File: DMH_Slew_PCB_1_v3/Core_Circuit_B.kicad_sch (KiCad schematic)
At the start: 48 parts, among them J6 TS_Jack_6.35mm_Sw, J60 Conn_01x08_PinHeader, J61 Conn_01x08_PinHeader, J7 TS_Jack_6.35mm_Sw, J8 TS_Jack_6.35mm_Sw, Q10 BC558, Q7 BC548, Q8 BC548, Q9 BC558, SW4 SW_DPDT_3way, SW5 SW_DPDT, SW6 SPDT_OnOffOn, U3 TL074, U4 TL074

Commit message: V3 sch redesign ongoing
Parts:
- removed J60, J61: Conn_01x08_PinHeader, Connector_PinHeader_2.54mm:PinHeader_1x08_P2.54mm_Vertical, symbol SynthStuff:Conn_01x08_PinHeader
- removed R69, R70: 1k, Resistor_THT:R_Axial_DIN0207_L6.3mm_D2.5mm_P7.62mm_Horizontal, symbol Device:R_US
- removed R71, R72: 100k, Resistor_THT:R_Axial_DIN0207_L6.3mm_D2.5mm_P7.62mm_Horizontal, symbol Device:R_US
- removed R73: 220k, Resistor_THT:R_Axial_DIN0207_L6.3mm_D2.5mm_P7.62mm_Horizontal, symbol Device:R_US
- removed R74: 10k, Resistor_THT:R_Axial_DIN0207_L6.3mm_D2.5mm_P7.62mm_Horizontal, symbol Device:R_US
- removed R75, R76: 1k8, Resistor_THT:R_Axial_DIN0207_L6.3mm_D2.5mm_P7.62mm_Horizontal, symbol Device:R_US
- added C17: 10pF, Capacitor_THT:C_Disc_D3.0mm_W2.0mm_P2.50mm, symbol Device:C
- added C18: 220nF, Capacitor_THT:C_Disc_D4.3mm_W1.9mm_P5.00mm, symbol Device:C
- added C19: 22nF, Capacitor_THT:C_Disc_D4.3mm_W1.9mm_P5.00mm, symbol Device:C
- added C20: 2.2nF, Capacitor_THT:C_Disc_D4.3mm_W1.9mm_P5.00mm, symbol Device:C
- added R41: 56k, Resistor_THT:R_Axial_DIN0207_L6.3mm_D2.5mm_P7.62mm_Horizontal, symbol Device:R_US
- added R42, R43, R44, R56: 100k, Resistor_THT:R_Axial_DIN0207_L6.3mm_D2.5mm_P7.62mm_Horizontal, symbol Device:R_US
- added R55: 220k, Resistor_THT:R_Axial_DIN0207_L6.3mm_D2.5mm_P7.62mm_Horizontal, symbol Device:R_US
- added R61, R62: 1k, Resistor_THT:R_Axial_DIN0207_L6.3mm_D2.5mm_P7.62mm_Horizontal, symbol Device:R_US
- added unit 5 of U3
- added unit 5 of U4
- C22: value 220nF -> 10pF; footprint Capacitor_THT:C_Disc_D4.3mm_W1.9mm_P5.00mm -> Capacitor_THT:C_Disc_D3.0mm_W2.0mm_P2.50mm
- C23: value 22nF -> 100nF
- C24: value 2.2nF -> 100nF
- C25, C26: value 10pF -> 100nF; footprint Capacitor_THT:C_Disc_D3.0mm_W2.0mm_P2.50mm -> Capacitor_THT:C_Disc_D4.3mm_W1.9mm_P5.00mm
- R46: value 56k -> 100k
- R47: value 100k -> 1k
- R52: value 1k -> 100k
- R53: value 100k -> 56k
- R58: value 56k -> 220k
- R59, R60: value 100k -> 1k8
- R63: value 220k -> 100k
- R65: value 100k -> 220k
- R66: value 220k -> 10k
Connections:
- net +10V_B: now also R58.1, R55.1; no longer R63.1, R66.1
- net GND: now also C23.2, C24.2, C25.1, C26.1, R51.2, R52.2, R59.1, R60.2, R64.2, R65.2; no longer R57.2, R59.2
- net at Q10.1 (C), Q7.1 (C), U4.13 (-): now also C22.1, R63.1; no longer C26.1
- net at Q10.2 (B): now also R68.1
- net at Q10.3 (E), Q7.3 (E), Q8.3 (E)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: now also R66.1
- net at Q8.1 (C), Q9.1 (C), U4.6 (-): now also C18.1, C19.1, C20.1; no longer C22.1, C23.1, C24.1
- net at C22.2: now also R66.2, U4.14; no longer SW6.3 (C)
- net at U4.8: now also C21.2, R63.2, R65.1; no longer C25.2
- net at RV4.3, SW4.2 (B): now also R53.2; no longer R58.2
- net B_CV_Buff_C: now reaches SW4.3 (C), SW4.4 (A)
- net B_CV_Buff_C: no longer U3.1, U3.2 (-)
- net at RV3.3, SW4.5 (B): now also R41.2; no longer R46.2
- net B_CV_In_Jack_M: now reaches J7.T
- net B_CV_In_Jack_M: no longer R52.2
- net at U4.9 (-): now also C21.1, R62.1; no longer C25.1
- net B_Rng_Sw_p1_C: now reaches SW6.1 (A)
- net B_Rng_Sw_p1_C: no longer C23.2
- net -12V: now reaches C26.2
- net -12V: now also C25.2, U3.11 (V-), U4.11 (V-); no longer U4.14
- net at U4.7: now also R61.2
- net Comp_-R renamed B_Comp_-R
- net B_Comp_-R: now also R67.2, R44.1; no longer R53.1
- removed net Comp_F: Q9.2 (B), R47.1, R65.2, R66.2, R68.1
- removed net Comp_R: Q7.2 (B), R60.1, R63.2, R64.2, R67.2
- removed net Fall_CV: R46.1, R65.1, RV3.2
- net In B TN renamed B_Input_Jack_TN_M
- removed net Input: J6.T, R54.2, U4.10 (+)
- net Out B TN renamed B_Out_Jack_TN_M
- removed net Output: C24.2, J8.T, R51.2, SW6.2 (B)
- removed net Rise_CV: R58.1, R64.1, RV4.2
- new net: R47.1, R51.1, U3.3 (+)
- new net: R48.1, R52.1, U4.3 (+)
- new net: C17.1, R43.2, R46.1, U4.2 (-)
- new net +12V: C23.1, C24.1, U3.4 (V+), U4.4 (V+)
- new net B_CV_Buff_S: U3.1, U3.2 (-)
- new net B_CV_In_Jack_S: R47.2
- new net B_Comp_F: Q9.2 (B), R42.1, R57.2, R58.2, R60.1
- new net B_Comp_R: Q7.2 (B), R54.1, R55.2, R56.2, R59.2
- new net B_Diff_Amp_C: SW5.1 (A)
- new net B_Diff_Amp_S: C17.2, R43.1, U4.1
- new net B_Fall_CV_C: R41.1, RV3.2
- new net B_Fall_CV_S: R57.1
- new net B_Input_Jack_M: J6.T
- new net B_Input_Jack_S: R48.2, R64.1, U4.10 (+)
- new net B_LinLog_Sw_p2_C: SW5.2 (B)
- new net B_LinLog_Sw_p2_S: R42.2, R44.2
- new net B_LinLog_Sw_p5_C: SW5.5 (B)
- new net B_LinLog_Sw_p5_S: R50.2, R54.2
- new net B_Out_Jack_C: SW6.2 (B)
- new net B_Out_Jack_M: J8.T
- new net B_Out_Jack_S: C20.2, R46.2, R61.1, R62.2
- new net B_Rise_CV_C: R53.1, RV4.2
- new net B_Rise_CV_S: R56.1
- new net B_Rng_Sw_p1_S: C19.2
- new net B_Rng_Sw_p3_C: SW6.3 (C)
- new net B_Rng_Sw_p3_S: C18.2
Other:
- note removed: "PCB 2"

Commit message: Finished PCB1 v3 schematic
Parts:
- added J21, J23, J24, J26: Conn_02x03_Top_Bottom, Connector_PinHeader_2.54mm:PinHeader_2x03_P2.54mm_Horizontal, symbol Connector_Generic:Conn_02x03_Top_Bottom
- added J22, J25: Conn_02x06_Top_Bottom, Connector_PinHeader_2.54mm:PinHeader_2x06_P2.54mm_Horizontal, symbol Connector_Generic:Conn_02x06_Top_Bottom
- added J27, J28, J29, J30: Conn_01x08, Connector_PinHeader_2.54mm:PinHeader_1x08_P2.54mm_Vertical, symbol Connector_Generic:Conn_01x08
- Q10, Q7, Q8, Q9: footprint Package_TO_SOT_THT:TO-92L_Inline_Wide -> Package_TO_SOT_THT:TO-92_Inline
- renumbered C25 to C24, C24 to C25
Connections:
- net +12V: now also J21.1 (Pin_1), J24.1 (Pin_1)
- net -12V: now also J21.4 (Pin_4), J24.4 (Pin_4)
- net B_CV_Buff_C: now also J29.6 (Pin_6)
- net B_CV_Buff_S: now also J22.4 (Pin_4)
- net B_CV_In_Jack_M: now also J26.5 (Pin_5)
- net B_CV_In_Jack_S: now also J23.5 (Pin_5)
- net B_Diff_Amp_C: now also J29.2 (Pin_2)
- net B_Diff_Amp_S: now also J22.1 (Pin_1)
- net B_Fall_CV_C: now also J29.4 (Pin_4)
- net B_Fall_CV_S: now also J22.3 (Pin_3)
- net B_Input_Jack_M: now also J26.4 (Pin_4)
- net B_Input_Jack_S: now also J23.4 (Pin_4)
- net B_LinLog_Sw_p2_C: now also J30.1 (Pin_1)
- net B_LinLog_Sw_p2_S: now also J22.7 (Pin_7)
- net B_LinLog_Sw_p5_C: now also J30.2 (Pin_2)
- net B_LinLog_Sw_p5_S: now also J22.8 (Pin_8)
- net B_Out_Jack_C: now also J30.6 (Pin_6)
- net B_Out_Jack_M: now also J26.6 (Pin_6), J28.6 (Pin_6)
- net B_Out_Jack_S: now also J23.6 (Pin_6)
- net B_Rise_CV_C: now also J29.3 (Pin_3)
- net B_Rise_CV_S: now also J22.2 (Pin_2)
- net B_Rng_Sw_p1_C: now also J30.7 (Pin_7)
- net B_Rng_Sw_p1_S: now also J22.12 (Pin_12)
- net B_Rng_Sw_p3_C: now also J30.5 (Pin_5)
- net B_Rng_Sw_p3_S: now also J22.11 (Pin_11)
- net GND: now also J21.3 (Pin_3), J21.5 (Pin_5), J21.6 (Pin_6), J22.5 (Pin_5), J22.6 (Pin_6), J23.3 (Pin_3), J24.3 (Pin_3), J24.5 (Pin_5), J24.6 (Pin_6), J25.5 (Pin_5), J25.6 (Pin_6), J26.3 (Pin_3), J27.1 (Pin_1), J27.7 (Pin_7), J27.8 (Pin_8), J28.8 (Pin_8), J29.1 (Pin_1), J29.7 (Pin_7), J29.8 (Pin_8), J30.8 (Pin_8)
- new net +10V_A: J21.2 (Pin_2), J24.2 (Pin_2), J27.5 (Pin_5), J29.5 (Pin_5)
- new net B_CV_Buff_M: J25.4 (Pin_4), J27.6 (Pin_6)
- new net B_Diff_Amp_M: J25.1 (Pin_1), J27.2 (Pin_2)
- new net B_F_Gate_Jack_M: J26.1 (Pin_1)
- new net B_F_Gate_Jack_S: J23.1 (Pin_1)
- new net B_F_LED_C: J30.3 (Pin_3)
- new net B_F_LED_M: J25.9 (Pin_9), J28.3 (Pin_3)
- new net B_F_LED_S: J22.9 (Pin_9)
- new net B_Fall_CV_M: J25.3 (Pin_3), J27.4 (Pin_4)
- new net B_LinLog_Sw_p2_M: J25.7 (Pin_7), J28.1 (Pin_1)
- new net B_LinLog_Sw_p5_M: J25.8 (Pin_8), J28.2 (Pin_2)
- new net B_R_Gate_Jack_M: J26.2 (Pin_2)
- new net B_R_Gate_Jack_S: J23.2 (Pin_2)
- new net B_R_LED_C: J30.4 (Pin_4)
- new net B_R_LED_M: J25.10 (Pin_10), J28.4 (Pin_4)
- new net B_R_LED_S: J22.10 (Pin_10)
- new net B_Rise_CV_M: J25.2 (Pin_2), J27.3 (Pin_3)
- new net B_Rng_Sw_p1_M: J25.12 (Pin_12), J28.7 (Pin_7)
- new net B_Rng_Sw_p3_M: J25.11 (Pin_11), J28.5 (Pin_5)
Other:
- moved on the sheet: C18, C19, C20, C21, C22, C23, C24, C25, C26, J6, J8, Q10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

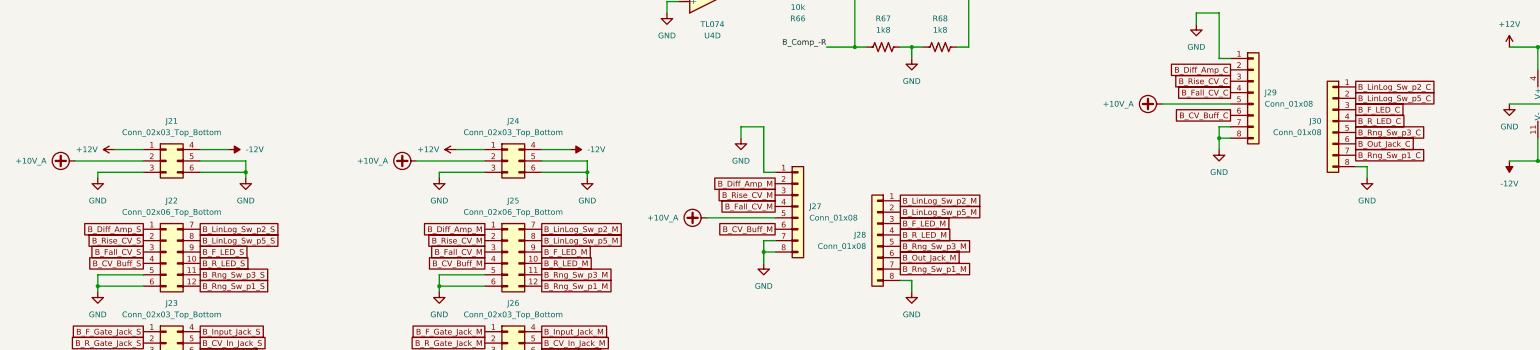
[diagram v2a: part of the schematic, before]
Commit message: Relinked PCB1 and 2 with new v3 schematics
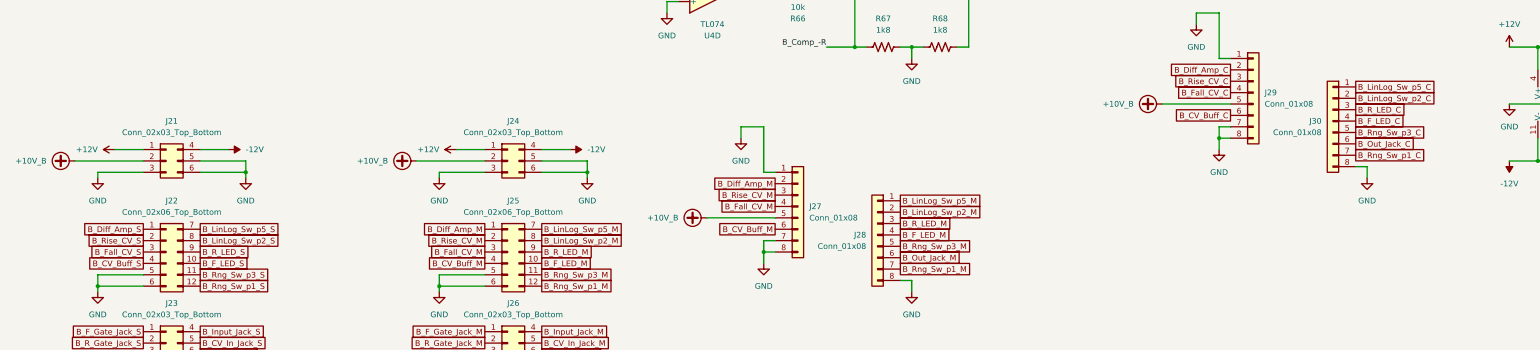
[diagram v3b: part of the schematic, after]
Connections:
- net +10V_A is gone; now on net +10V_B: J21.2 (Pin_2), J24.2 (Pin_2), J27.5 (Pin_5), J29.5 (Pin_5)
- net B_F_LED_C: now also J30.4 (Pin_4); no longer J30.3 (Pin_3)
- net B_F_LED_M: now also J25.10 (Pin_10), J28.4 (Pin_4); no longer J25.9 (Pin_9), J28.3 (Pin_3)
- net B_F_LED_S: now also J22.10 (Pin_10); no longer J22.9 (Pin_9)
- net B_LinLog_Sw_p2_C: now also J30.2 (Pin_2); no longer J30.1 (Pin_1)
- net B_LinLog_Sw_p2_M: now also J25.8 (Pin_8), J28.2 (Pin_2); no longer J25.7 (Pin_7), J28.1 (Pin_1)
- net B_LinLog_Sw_p2_S: now also J22.8 (Pin_8); no longer J22.7 (Pin_7)
- net B_LinLog_Sw_p5_C: now also J30.1 (Pin_1); no longer J30.2 (Pin_2)
- net B_LinLog_Sw_p5_M: now also J25.7 (Pin_7), J28.1 (Pin_1); no longer J25.8 (Pin_8), J28.2 (Pin_2)
- net B_LinLog_Sw_p5_S: now also J22.7 (Pin_7); no longer J22.8 (Pin_8)
- net B_R_LED_C: now also J30.3 (Pin_3); no longer J30.4 (Pin_4)
- net B_R_LED_M: now also J25.9 (Pin_9), J28.3 (Pin_3); no longer J25.10 (Pin_10), J28.4 (Pin_4)
- net B_R_LED_S: now also J22.9 (Pin_9); no longer J22.10 (Pin_10)

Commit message: PCB 1 component placement done
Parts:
- J24, J26: footprint Connector_PinHeader_2.54mm:PinHeader_2x03_P2.54mm_Horizontal -> Connector_PinSocket_2.54mm:PinSocket_2x03_P2.54mm_Vertical
- J25: footprint Connector_PinHeader_2.54mm:PinHeader_2x06_P2.54mm_Horizontal -> Connector_PinSocket_2.54mm:PinSocket_2x06_P2.54mm_Vertical
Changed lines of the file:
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@@
 			)
 		)
-		(property "Footprint" "Connector_PinHeader_2.54mm:PinHeader_2x03_P2.54mm_Horizontal"
+		(property "Footprint" "Connector_PinSocket_2.54mm:PinSocket_2x03_P2.54mm_Vertical"
 			(at 125.73 228.6 0)
 			(effects
@@
 			)
 		)
+		(property "Function" ""
+			(at 125.73 228.6 0)
+			(effects
+				(font
+					(size 1.27 1.27)
+				)
+			)
+		)
 		(pin "5"
 		)
@@
 			)
 		)
-		(property "Footprint" "Connector_PinHeader_2.54mm:PinHeader_2x03_P2.54mm_Horizontal"
+		(property "Footprint" "Connector_PinSocket_2.54mm:PinSocket_2x03_P2.54mm_Vertical"
 			(at 125.73 269.24 0)
 			(effects
@@
 			)
 		)
+		(property "Function" ""
+			(at 125.73 269.24 0)
+			(effects
+				(font
+					(size 1.27 1.27)
+				)
+			)
+		)
 		(pin "5"
 		)
@@
 			)
 		)
-		(property "Footprint" "Connector_PinHeader_2.54mm:PinHeader_2x06_P2.54mm_Horizontal"
+		(property "Footprint" "Connector_PinSocket_2.54mm:PinSocket_2x06_P2.54mm_Vertical"
 			(at 125.73 248.92 0)
 			(effects
@@
 			)
 		)
+		(property "Function" ""
+			(at 125.73 248.92 0)
+			(effects
+				(font
+					(size 1.27 1.27)
+				)
+			)
+		)

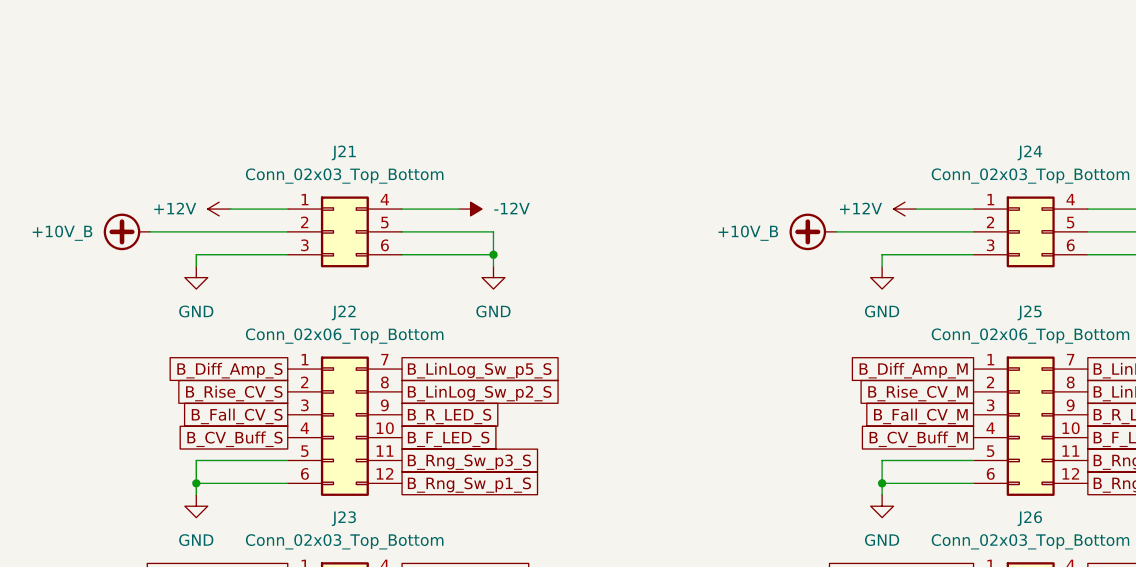
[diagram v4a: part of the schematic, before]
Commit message: PCB 1 routing in progress
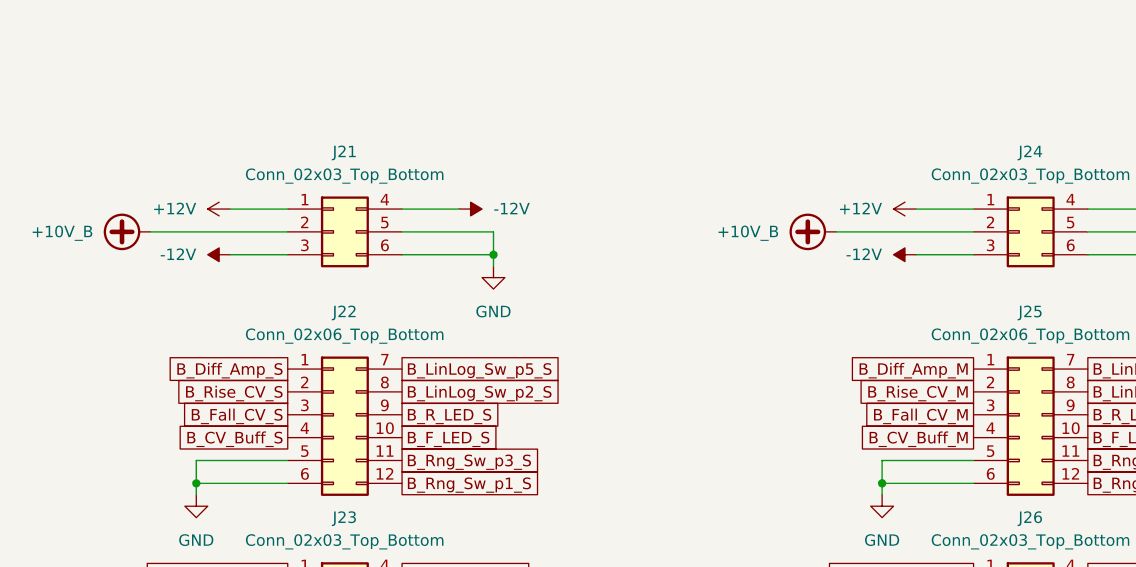
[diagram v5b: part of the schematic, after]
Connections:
- net -12V: now also J21.3 (Pin_3), J24.3 (Pin_3)
- net GND: no longer J21.3 (Pin_3), J24.3 (Pin_3)
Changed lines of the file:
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@@
 	(wire
 		(pts
-			(xy 34.29 231.14) (xy 44.45 231.14)
+			(xy 38.1 231.14) (xy 44.45 231.14)
 		)
 		(stroke
@@
 	(wire
 		(pts
-			(xy 34.29 232.41) (xy 34.29 231.14)
-		)
-		(stroke
-			(width 0)
-			(type default)
-		)
-	)
-	(wire
-		(pts
 			(xy 129.54 74.93) (xy 129.54 72.39)
 		)
@@
 	(wire
 		(pts
-			(xy 120.65 231.14) (xy 110.49 231.14)
+			(xy 120.65 231.14) (xy 114.3 231.14)
 		)
 		(stroke
@@
 	(wire
 		(pts
-			(xy 110.49 231.14) (xy 110.49 232.41)
-		)
-		(stroke
-			(width 0)
-			(type default)
-		)
-	)
-	(wire
-		(pts
 			(xy 292.1 67.31) (xy 292.1 77.47)
 		)
@@
 	)
 	(symbol
-		(lib_id "power:GND")
-		(at 34.29 232.41 0)
-		(mirror y)
-		(unit 1)
-		(exclude_from_sim no)
-		(in_bom yes)
-		(on_board no)
-		(dnp no)
-		(fields_autoplaced yes)
-		(property "Reference" "#PWR0106"
-			(at 34.29 238.76 0)
-			(effects
-				(font
-					(size 1.27 1.27)
-				)
-				(hide yes)
-			)
-		)
-		(property "Value" "GND"
-			(at 34.29 237.49 0)
-			(effects
-				(font
-					(size 1.27 1.27)
-				)
-			)
-		)
-		(property "Footprint" ""
-			(at 34.29 232.41 0)
-			(effects
-				(font
-					(size 1.27 1.27)
-				)
-				(hide yes)
-			)
-		)
-		(property "Datasheet" ""
-			(at 34.29 232.41 0)
-			(effects
-				(font
-					(size 1.27 1.27)
-				)
-				(hide yes)
-			)
-		)
-		(property "Description" "Power symbol creates a global label with name \"GND\" , ground"
-			(at 34.29 232.41 0)
-			(effects
-				(font
-					(size 1.27 1.27)
-				)
-				(hide yes)
-			)
-		)
-		(pin "1"
-		)
-		(instances
-			(project "DMH_Slew_PCB_1_v3"
-				(path "/58f4306d-5387-4983-bb08-41a2313fd315/77d402a4-d1d6-4e9c-af86-3ca5793147b8"
-					(reference "#PWR0106")
-					(unit 1)
-				)
-			)
-		)
-	)
-	(symbol
 		(lib_id "Transistor_BJT:BC558")
 		(at 228.6 173.99 270)
@@
 	)
 	(symbol
+		(lib_id "power:-12V")
+		(at 38.1 231.14 90)
+		(unit 1)
+		(exclude_from_sim no)
+		(in_bom yes)
+		(on_board no)
+		(dnp no)
+		(fields_autoplaced yes)
+		(property "Reference" "#PWR0106"
+			(at 41.91 231.14 0)
+			(effects
+				(font
+					(size 1.27 1.27)
+				)
+				(hide yes)
+			)
+		)
+		(property "Value" "-12V"
+			(at 34.29 231.1399 90)
+			(effects
+				(font
+					(size 1.27 1.27)
+				)
+				(justify left)
+			)
+		)
+		(property "Footprint" ""
+			(at 38.1 231.14 0)
+			(effects
+				(font
+					(size 1.27 1.27)
+				)
+				(hide yes)
+			)
+		)
+		(property "Datasheet" ""
+			(at 38.1 231.14 0)
+			(effects
+				(font
+					(size 1.27 1.27)
+				)
+				(hide yes)
+			)
+		)
+		(property "Description" "Power symbol creates a global label with name \"-12V\""
+			(at 38.1 231.14 0)
+			(effects
+				(font
+					(size 1.27 1.27)
+				)
+				(hide yes)
+			)
+		)
+		(pin "1"
+		)
+		(instances
+			(project "DMH_Slew_PCB_1_v3"
+				(path "/58f4306d-5387-4983-bb08-41a2313fd315/77d402a4-d1d6-4e9c-af86-3ca5793147b8"
+					(reference "#PWR0106")
+					(unit 1)
+				)
+			)
+		)
+	)
+	(symbol
 		(lib_id "power:GND")
 		(at 180.34 93.98 0)
@@
 	)
 	(symbol
+		(lib_id "power:-12V")
+		(at 114.3 231.14 90)
+		(unit 1)
+		(exclude_from_sim no)
+		(in_bom yes)
+		(on_board yes)
+		(dnp no)
+		(fields_autoplaced yes)
+		(property "Reference" "#PWR0113"
+			(at 118.11 231.14 0)
+			(effects
+				(font
+					(size 1.27 1.27)
+				)
+				(hide yes)
+			)
+		)
+		(property "Value" "-12V"
+			(at 110.49 231.1399 90)
+			(effects
+				(font
+					(size 1.27 1.27)
+				)
+				(justify left)
+			)
+		)
+		(property "Footprint" ""
+			(at 114.3 231.14 0)
+			(effects
+				(font
+					(size 1.27 1.27)
+				)
+				(hide yes)
+			)
+		)
+		(property "Datasheet" ""
+			(at 114.3 231.14 0)
+			(effects
+				(font
+					(size 1.27 1.27)
+				)
+				(hide yes)
+			)
+		)
+		(property "Description" "Power symbol creates a global label with name \"-12V\""
+			(at 114.3 231.14 0)
+			(effects
+				(font
+					(size 1.27 1.27)
+				)
+				(hide yes)
+			)
+		)
+		(pin "1"
+		)
+		(instances
+			(project "DMH_Slew_PCB_1_v3"
+				(path "/58f4306d-5387-4983-bb08-41a2313fd315/77d402a4-d1d6-4e9c-af86-3ca5793147b8"
+					(reference "#PWR0113")
+					(unit 1)
+				)
+			)
+		)
+	)
+	(symbol
 		(lib_id "power:GND")
 		(at 180.34 76.2 0)
@@
 					(unit 1)
 				)
-			)
-		)
-	)
-	(symbol
-		(lib_id "power:GND")
-		(at 110.49 232.41 0)
-		(unit 1)
-		(exclude_from_sim no)
-		(in_bom yes)
-		(on_board yes)
-		(dnp no)
-		(fields_autoplaced yes)
-		(property "Reference" "#PWR0113"
-			(at 110.49 238.76 0)
-			(effects
-				(font
-					(size 1.27 1.27)
-				)
-				(hide yes)
-			)
-		)
-		(property "Value" "GND"
-			(at 110.49 237.49 0)
-			(effects
-				(font
-					(size 1.27 1.27)
-				)
-			)
-		)
-		(property "Footprint" ""
-			(at 110.49 232.41 0)
-			(effects
-				(font
-					(size 1.27 1.27)
-				)
-				(hide yes)
-			)
-		)
-		(property "Datasheet" ""
-			(at 110.49 232.41 0)
-			(effects
-				(font
-					(size 1.27 1.27)
-				)
-				(hide yes)
-			)
-		)
-		(property "Description" "Power symbol creates a global label with name \"GND\" , ground"
-			(at 110.49 232.41 0)
-			(effects
-				(font
-					(size 1.27 1.27)
-				)
-				(hide yes)
-			)
-		)
-		(pin "1"
-		)
-		(instances
-			(project "DMH_Slew_PCB_1_v3"
-				(path "/58f4306d-5387-4983-bb08-41a2313fd315/77d402a4-d1d6-4e9c-af86-3ca5793147b8"
-					(reference "#PWR0113")
-					(unit 1)
-				)
